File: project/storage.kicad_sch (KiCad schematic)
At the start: 54 parts

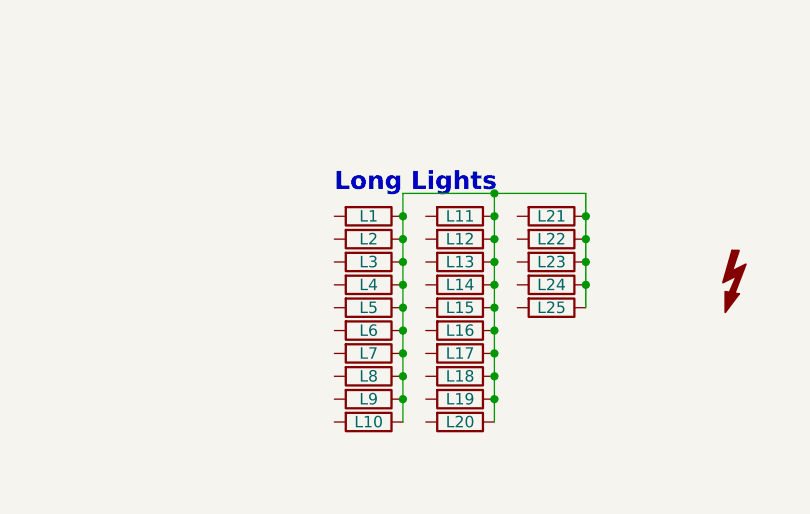
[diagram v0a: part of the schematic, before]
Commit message: adding few light fixtured in storage area
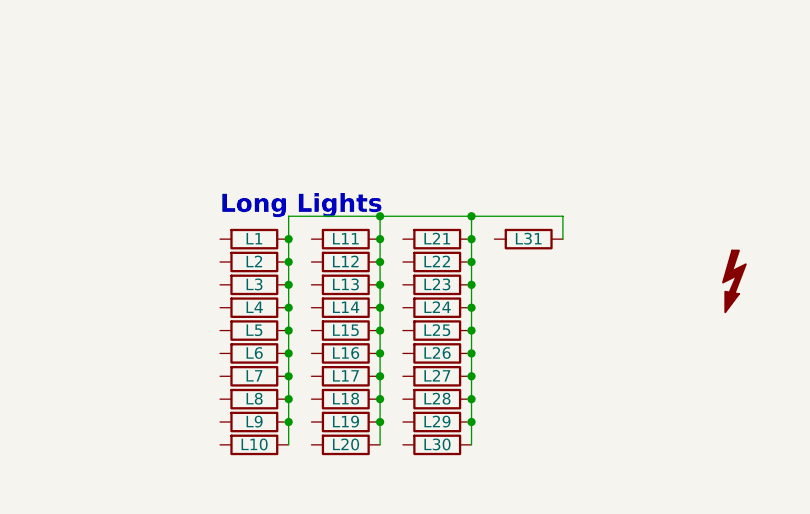
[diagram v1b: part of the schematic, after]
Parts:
- added L26, L27, L28, L29, L30, L31: light, -local:light_long, symbol Device:R
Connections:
- net at L1.1, L10.1, L11.1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: now also L26.1, L27.1, L28.1, L29.1, L30.1, L31.1
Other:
- moved on the sheet: L1, L10, L11, L12, L13, L14, L15, L16, L17, L18, L19, L2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
